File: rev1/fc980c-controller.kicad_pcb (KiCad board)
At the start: 2 copper layers, 82.2 x 35.5 mm, 34 parts, among them J1 SWD, J2 USB, J3 KEYBOARD, SW1 BOOT0, U1 XC6206P332MR, U2 STM32F401CBUx, U3 USBLC6-2SC6, U4 M24C64-RMN6TP, U5 PCA9306DC, Y1 8MHz Cl 20pF

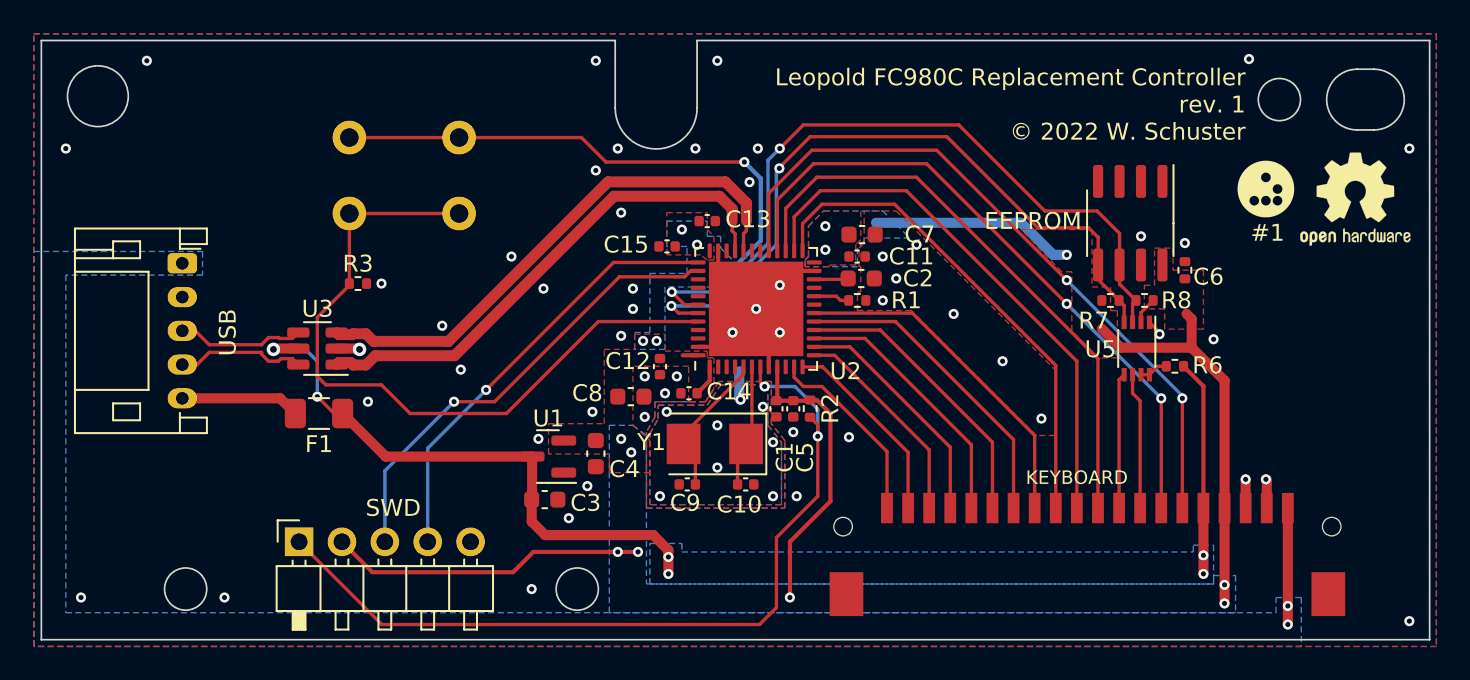
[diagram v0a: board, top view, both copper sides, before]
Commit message: rev1: Minor tweaks before first production run
Most notably change to a capacitor footprint rather than resistor
footprint for C6.

Small via tweaks.

Adjust component rotations reviewing JLC SMTA preview. (still waiting on
JLC review at this point)
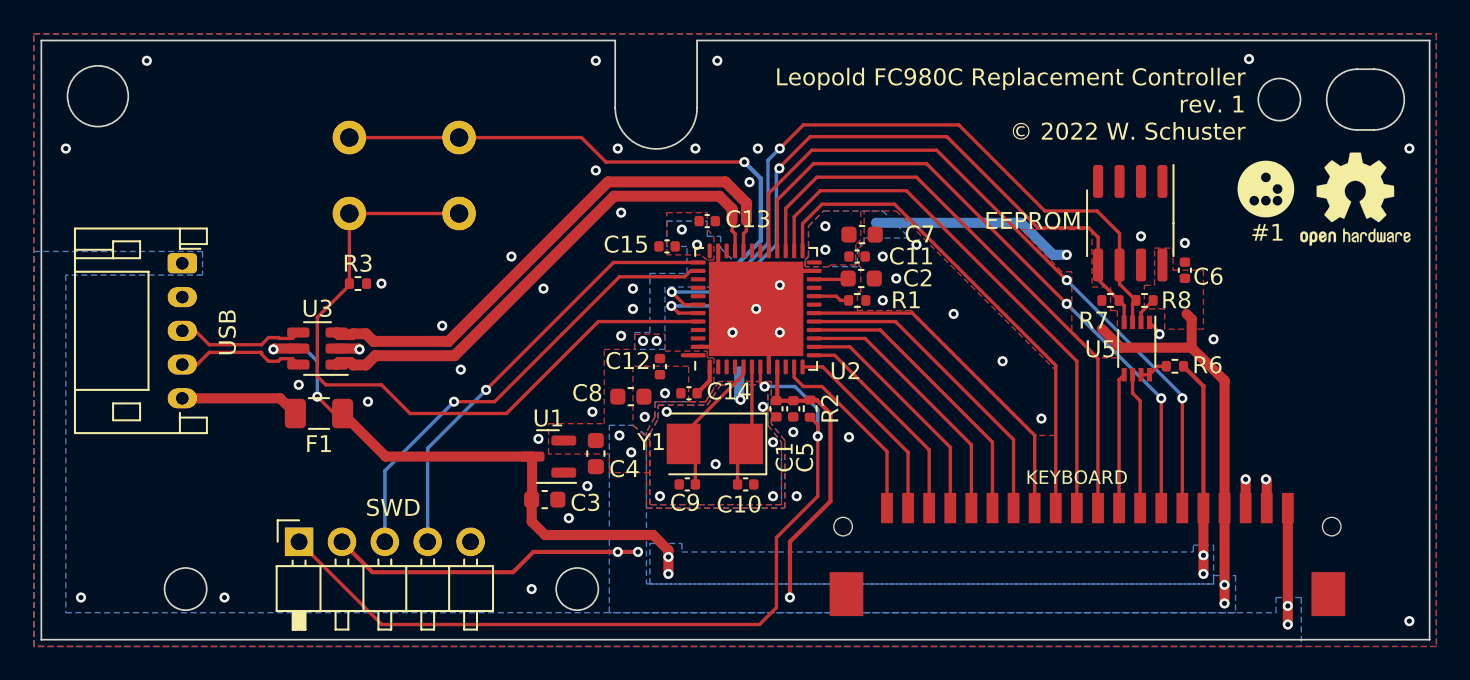
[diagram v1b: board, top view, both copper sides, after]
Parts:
- C6: footprint Resistor_SMD:R_0402_1005Metric -> Capacitor_SMD:C_0402_1005Metric
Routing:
- net GND: vias 62 -> 60
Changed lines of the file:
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@@
     (property "Sheetfile" "fc980c-controller.kicad_sch")
     (property "Sheetname" "")
-    (attr exclude_from_pos_files exclude_from_bom)
+    (attr exclude_from_pos_files)
     (fp_text reference "LOGO1" (at 0 0) (layer "F.SilkS") hide
       (effects (font (size 1 1) (thickness 0.15)))
@@
     )
   )
-  (footprint "Resistor_SMD:R_0402_1005Metric" (layer "F.Cu")
+  (footprint "Capacitor_SMD:C_0402_1005Metric" (layer "F.Cu")
     (at 142.5 49.11 90)
-    (descr "Resistor SMD 0402 (1005 Metric), square (rectangular) end terminal, IPC_7351 nominal, (Body size source: IPC-SM-782 page 72, https://www.pcb-3d.com/wordpress/wp-content/uploads/ipc-sm-782a_amendment_1_and_2.pdf), generated with kicad-footprint-generator")
-    (tags "resistor")
+    (descr "Capacitor SMD 0402 (1005 Metric), square (rectangular) end terminal, IPC_7351 nominal, (Body size source: IPC-SM-782 page 76, https://www.pcb-3d.com/wordpress/wp-content/uploads/ipc-sm-782a_amendment_1_and_2.pdf), generated with kicad-footprint-generator")
+    (tags "capacitor")
     (property "Sheetfile" "fc980c-controller.kicad_sch")
     (property "Sheetname" "")
@@
       (effects (font (size 1 1) (thickness 0.15)))
     )
-    (fp_text value "100nF" (at 0 1.17 90) (layer "F.Fab")
+    (fp_text value "100nF" (at 0 1.16 90) (layer "F.Fab")
       (effects (font (size 1 1) (thickness 0.15)))
     )
     (fp_text user "${REFERENCE}" (at 0 0 90) (layer "F.Fab")
-      (effects (font (size 0.26 0.26) (thickness 0.04)))
+      (effects (font (size 0.25 0.25) (thickness 0.04)))
     )
-    (fp_line (start -0.153641 0.38) (end 0.153641 0.38) (layer "F.SilkS") (width 0.12))
-    (fp_line (start -0.153641 -0.38) (end 0.153641 -0.38) (layer "F.SilkS") (width 0.12))
-    (fp_line (start -0.93 0.47) (end -0.93 -0.47) (layer "F.CrtYd") (width 0.05))
-    (fp_line (start 0.93 0.47) (end -0.93 0.47) (layer "F.CrtYd") (width 0.05))
-    (fp_line (start -0.93 -0.47) (end 0.93 -0.47) (layer "F.CrtYd") (width 0.05))
-    (fp_line (start 0.93 -0.47) (end 0.93 0.47) (layer "F.CrtYd") (width 0.05))
-    (fp_line (start -0.525 0.27) (end -0.525 -0.27) (layer "F.Fab") (width 0.1))
-    (fp_line (start 0.525 -0.27) (end 0.525 0.27) (layer "F.Fab") (width 0.1))
-    (fp_line (start -0.525 -0.27) (end 0.525 -0.27) (layer "F.Fab") (width 0.1))
-    (fp_line (start 0.525 0.27) (end -0.525 0.27) (layer "F.Fab") (width 0.1))
-    (pad "1" smd roundrect (at -0.51 0 90) (size 0.54 0.64) (layers "F.Cu" "F.Paste" "F.Mask") (roundrect_rratio 0.25)
+    (fp_line (start -0.107836 -0.36) (end 0.107836 -0.36) (layer "F.SilkS") (width 0.12))
+    (fp_line (start -0.107836 0.36) (end 0.107836 0.36) (layer "F.SilkS") (width 0.12))
+    (fp_line (start 0.91 -0.46) (end 0.91 0.46) (layer "F.CrtYd") (width 0.05))
+    (fp_line (start -0.91 -0.46) (end 0.91 -0.46) (layer "F.CrtYd") (width 0.05))
+    (fp_line (start 0.91 0.46) (end -0.91 0.46) (layer "F.CrtYd") (width 0.05))
+    (fp_line (start -0.91 0.46) (end -0.91 -0.46) (layer "F.CrtYd") (width 0.05))
+    (fp_line (start -0.5 -0.25) (end 0.5 -0.25) (layer "F.Fab") (width 0.1))
+    (fp_line (start 0.5 -0.25) (end 0.5 0.25) (layer "F.Fab") (width 0.1))
+    (fp_line (start 0.5 0.25) (end -0.5 0.25) (layer "F.Fab") (width 0.1))
+    (fp_line (start -0.5 0.25) (end -0.5 -0.25) (layer "F.Fab") (width 0.1))
+    (pad "1" smd roundrect (at -0.48 0 90) (size 0.56 0.62) (layers "F.Cu" "F.Paste" "F.Mask") (roundrect_rratio 0.25)
       (net 2 "VDDA") (pintype "passive"))
-    (pad "2" smd roundrect (at 0.51 0 90) (size 0.54 0.64) (layers "F.Cu" "F.Paste" "F.Mask") (roundrect_rratio 0.25)
+    (pad "2" smd roundrect (at 0.48 0 90) (size 0.56 0.62) (layers "F.Cu" "F.Paste" "F.Mask") (roundrect_rratio 0.25)
       (net 1 "GND") (pintype "passive"))
-    (model "${KICAD6_3DMODEL_DIR}/Resistor_SMD.3dshapes/R_0402_1005Metric.wrl"
+    (model "${KICAD6_3DMODEL_DIR}/Capacitor_SMD.3dshapes/C_0402_1005Metric.wrl"
       (offset (xyz 0 0 0))
       (scale (xyz 1 1 1))
@@
   (via (at 102.6 48.3) (size 0.6) (drill 0.3) (layers "F.Cu" "B.Cu") (free) (net 1))
   (via (at 98.5 52.4) (size 0.6) (drill 0.3) (layers "F.Cu" "B.Cu") (free) (net 1))
-  (via (at 110.5 55.4) (size 0.6) (drill 0.3) (layers "F.Cu" "B.Cu") (free) (net 1))
   (via (at 106 63.8) (size 0.6) (drill 0.3) (layers "F.Cu" "B.Cu") (free) (net 1))
   (via (at 124.6 48.3) (size 0.6) (drill 0.3) (layers "F.Cu" "B.Cu") (free) (net 1))
@@
   (via (at 107.1 61.9) (size 0.6) (drill 0.3) (layers "F.Cu" "B.Cu") (free) (net 1))
   (via (at 141 52.9) (size 0.6) (drill 0.3) (layers "F.Cu" "B.Cu") (net 1))
-  (via (at 114.8 58.3) (size 0.6) (drill 0.3) (layers "F.Cu" "B.Cu") (free) (net 1))
   (via (at 155.8 69.9) (size 0.6) (drill 0.3) (layers "F.Cu" "B.Cu") (free) (net 1))
   (via (at 147.3 61.5) (size 0.6) (drill 0.3) (layers "F.Cu" "B.Cu") (net 1))
@@
   (via (at 146.3 36.6) (size 0.6) (drill 0.3) (layers "F.Cu" "B.Cu") (free) (net 1))
   (via (at 76.2 41.9) (size 0.6) (drill 0.3) (layers "F.Cu" "B.Cu") (free) (net 1))
+  (via (at 90 55.9) (size 0.6) (drill 0.3) (layers "F.Cu" "B.Cu") (free) (net 1))
   (via (at 116.176089 56.776089) (size 0.6) (drill 0.3) (layers "F.Cu" "B.Cu") (free) (net 1))
   (via (at 77.1 68.5) (size 0.6) (drill 0.3) (layers "F.Cu" "B.Cu") (free) (net 1))
-  (via (at 93.6 53.8) (size 0.8) (drill 0.4) (layers "F.Cu" "B.Cu") (net 1))
+  (via (at 93.6 53.8) (size 0.6) (drill 0.3) (layers "F.Cu" "B.Cu") (net 1))
   (via (at 118.1 62.5) (size 0.6) (drill 0.3) (layers "F.Cu" "B.Cu") (free) (net 1))
   (via (at 144.2 53.2) (size 0.6) (drill 0.3) (layers "F.Cu" "B.Cu") (free) (net 1))
@@
   (via (at 111.8 57.5) (size 0.6) (drill 0.3) (layers "F.Cu" "B.Cu") (free) (net 1))
   (via (at 131.7 54.5) (size 0.6) (drill 0.3) (layers "F.Cu" "B.Cu") (free) (net 1))
-  (via (at 114.8 60.8) (size 0.6) (drill 0.3) (layers "F.Cu" "B.Cu") (free) (net 1))
+  (via (at 114.7 60.6) (size 0.6) (drill 0.3) (layers "F.Cu" "B.Cu") (free) (net 1))
   (via (at 126.6 47.6) (size 0.6) (drill 0.3) (layers "F.Cu" "B.Cu") (free) (net 1))
   (via (at 109.1 45.7) (size 0.6) (drill 0.3) (layers "F.Cu" "B.Cu") (free) (net 1))
   (via (at 108.9 41.9) (size 0.6) (drill 0.3) (layers "F.Cu" "B.Cu") (free) (net 1))
   (via (at 99.6 55) (size 0.6) (drill 0.3) (layers "F.Cu" "B.Cu") (free) (net 1))
-  (via (at 112.4 55.4) (size 0.6) (drill 0.3) (layers "F.Cu" "B.Cu") (free) (net 1))
   (via (at 134 57.9) (size 0.6) (drill 0.3) (layers "F.Cu" "B.Cu") (free) (net 1))
   (via (at 119.5 62.5) (size 0.6) (drill 0.3) (layers "F.Cu" "B.Cu") (free) (net 1))
@@
   (via (at 135.5 48.2) (size 0.6) (drill 0.3) (layers "F.Cu" "B.Cu") (net 2))
   (via (at 144.85 67.75) (size 0.6) (drill 0.3) (layers "F.Cu" "B.Cu") (free) (net 2))
-  (via (at 109.1 59.1) (size 0.6) (drill 0.3) (layers "F.Cu" "B.Cu") (free) (net 2))
+  (via (at 109 58.9) (size 0.6) (drill 0.3) (layers "F.Cu" "B.Cu") (free) (net 2))
   (via (at 110.1 65.8) (size 0.6) (drill 0.3) (layers "F.Cu" "B.Cu") (net 2))
   (via (at 121.2 46.5) (size 0.6) (drill 0.3) (layers "F.Cu" "B.Cu") (free) (net 2))
@@
   (via (at 91.1 56.6) (size 0.6) (drill 0.3) (layers "F.Cu" "B.Cu") (net 3))
   (via (at 111.9 66.1) (size 0.6) (drill 0.3) (layers "F.Cu" "B.Cu") (net 3))
-  (via (at 88.5 53.8) (size 0.8) (drill 0.4) (layers "F.Cu" "B.Cu") (net 3))
+  (via (at 88.5 53.8) (size 0.6) (drill 0.3) (layers "F.Cu" "B.Cu") (net 3))
   (via (at 143.6 67.1) (size 0.6) (drill 0.3) (layers "F.Cu" "B.Cu") (free) (net 3))
   (via (at 111.9 67.1) (size 0.6) (drill 0.3) (layers "F.Cu" "B.Cu") (net 3))

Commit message: rev1: Final production files for first run
Last tweak is to add tooling holes necessary for JLC PCB assembly. JLC
will place them on their own, however in their first attempt put one
hole over the silkscreen, so placing them manually should prevent this
in the future.
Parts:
- added H1: JLC tooling hole, additional:JLC_tooling_hole, F.Cu at (154.6, 67.2)
- added H2: JLC tooling hole, additional:JLC_tooling_hole, F.Cu at (81.3, 41.0)
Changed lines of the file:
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@@
     (property "Sheetfile" "fc980c-controller.kicad_sch")
     (property "Sheetname" "")
-    (attr exclude_from_pos_files)
+    (attr exclude_from_pos_files exclude_from_bom)
     (fp_text reference "LOGO1" (at 0 0) (layer "F.SilkS") hide
       (effects (font (size 1 1) (thickness 0.15)))
@@
     )
   )
+  (footprint "additional:JLC_tooling_hole" (layer "F.Cu")
+    (at 81.3 41)
+    (descr "Mounting Hole 2.1mm, no annular")
+    (tags "mounting hole 2.1mm no annular")
+    (property "Sheetfile" "fc980c-controller.kicad_sch")
+    (property "Sheetname" "")
+    (attr exclude_from_pos_files exclude_from_bom)
+    (fp_text reference "H2" (at 0 -3.2) (layer "F.SilkS") hide
+      (effects (font (size 1 1) (thickness 0.15)))
+    )
+    (fp_text value "JLC tooling hole" (at 0 3.2) (layer "F.Fab")
+      (effects (font (size 1 1) (thickness 0.15)))
+    )
+    (fp_text user "${REFERENCE}" (at 0.3 0) (layer "F.Fab")
+      (effects (font (size 1 1) (thickness 0.15)))
+    )
+    (fp_circle (center 0 0) (end 2.1 0) (layer "Cmts.User") (width 0.15) (fill none))
+    (fp_circle (center 0 0) (end 2.35 0) (layer "F.CrtYd") (width 0.05) (fill none))
+    (pad "" np_thru_hole circle locked (at 0 0) (size 1.152 1.152) (drill 1.152) (layers *.Cu *.Mask)
+      (solder_mask_margin 0.148) (solder_paste_margin 1.152) (zone_connect 0))
+  )
   (footprint "Capacitor_SMD:C_0603_1608Metric" (layer "F.Cu")
     (at 107.6 59.975 -90)
@@
     )
   )
+  (footprint "additional:JLC_tooling_hole" (layer "F.Cu")
+    (at 154.6 67.2)
+    (descr "Mounting Hole 2.1mm, no annular")
+    (tags "mounting hole 2.1mm no annular")
+    (property "Sheetfile" "fc980c-controller.kicad_sch")
+    (property "Sheetname" "")
+    (attr exclude_from_pos_files exclude_from_bom)
+    (fp_text reference "H1" (at 0 -3.2) (layer "F.SilkS") hide
+      (effects (font (size 1 1) (thickness 0.15)))
+    )
+    (fp_text value "JLC tooling hole" (at 0 3.2) (layer "F.Fab")
+      (effects (font (size 1 1) (thickness 0.15)))
+    )
+    (fp_text user "${REFERENCE}" (at 0.3 0) (layer "F.Fab")
+      (effects (font (size 1 1) (thickness 0.15)))
+    )
+    (fp_circle (center 0 0) (end 2.1 0) (layer "Cmts.User") (width 0.15) (fill none))
+    (fp_circle (center 0 0) (end 2.35 0) (layer "F.CrtYd") (width 0.05) (fill none))
+    (pad "" np_thru_hole circle locked (at 0 0) (size 1.152 1.152) (drill 1.152) (layers *.Cu *.Mask)
+      (solder_mask_margin 0.148) (solder_paste_margin 1.152) (zone_connect 0))
+  )
   (footprint "Capacitor_SMD:C_0402_1005Metric" (layer "F.Cu")
